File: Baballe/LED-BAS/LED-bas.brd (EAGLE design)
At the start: 30 x 32 mm, 12 parts, among them Q1 200mA/50V, Q2 200mA/50V, Q3 200mA/50V

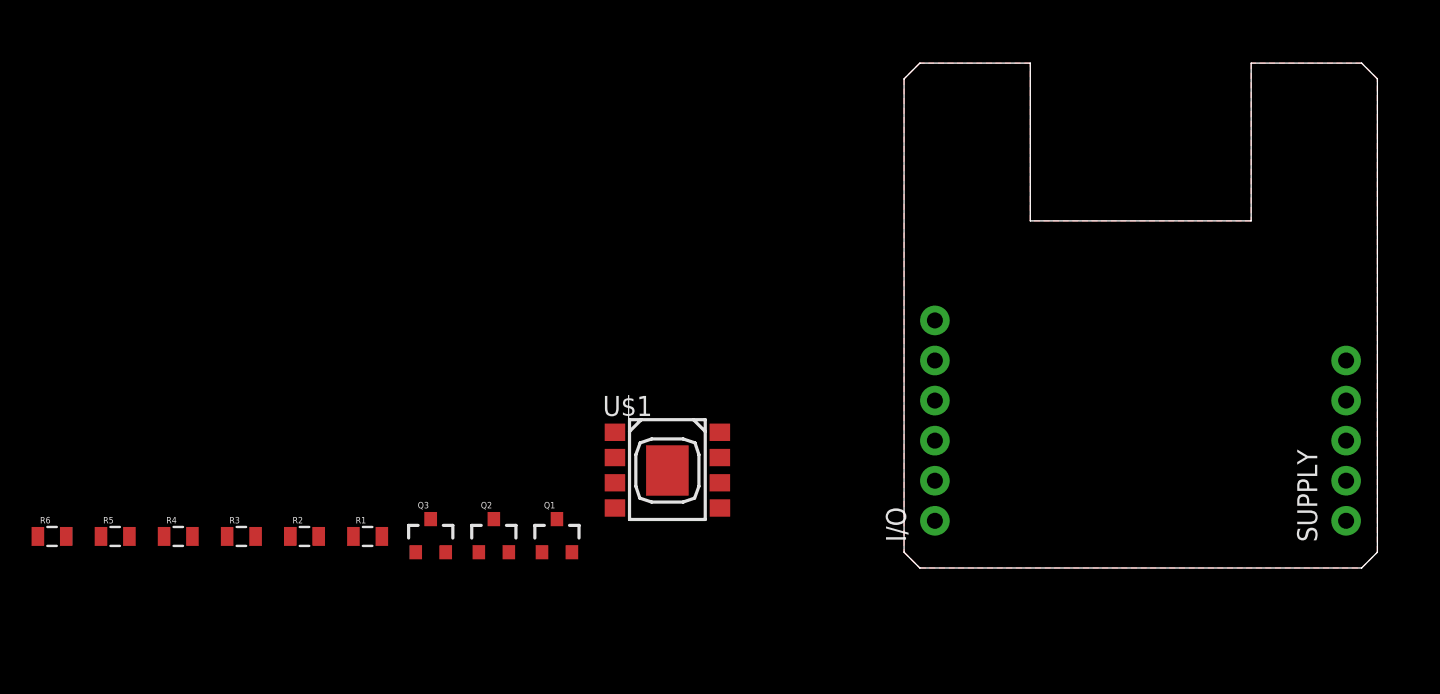
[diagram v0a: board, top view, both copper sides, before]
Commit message: Modification sur les modules led et alimentation
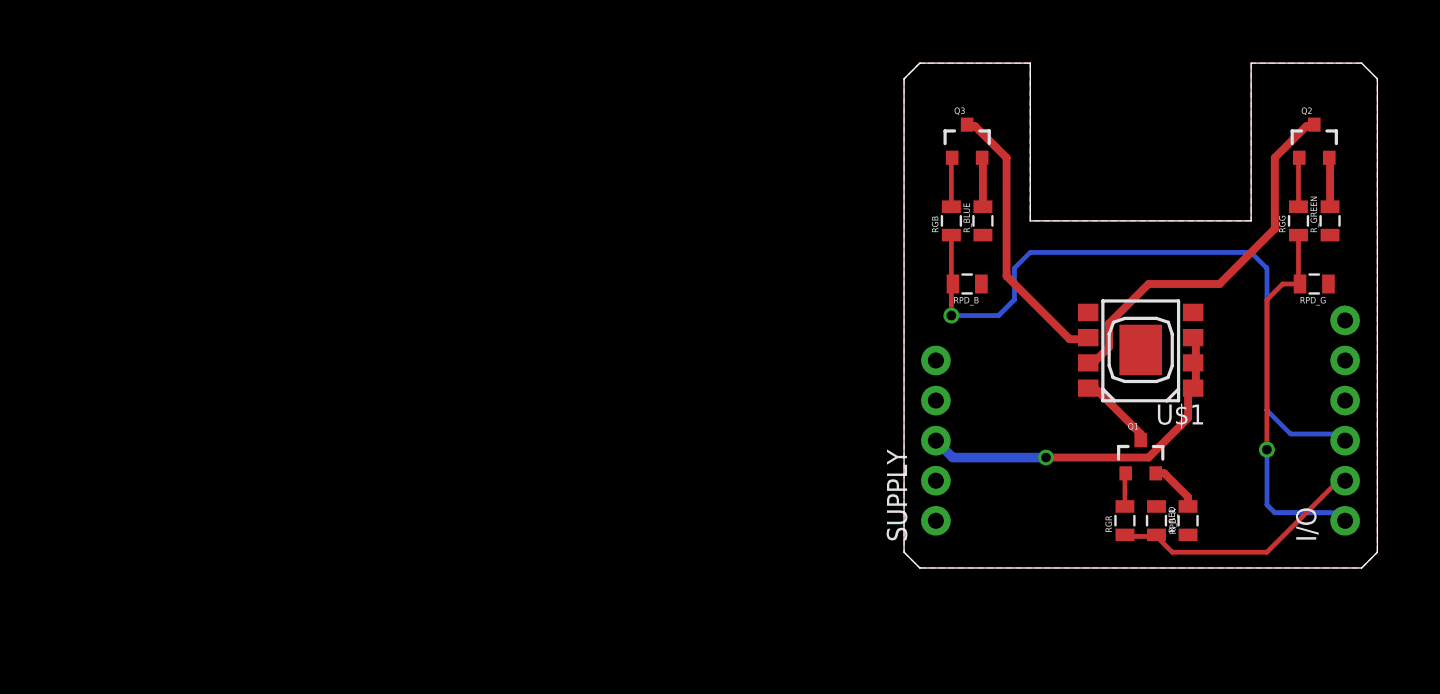
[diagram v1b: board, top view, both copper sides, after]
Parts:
- removed R1, R2, R3, R4, R5, R6: (no value), SparkFun-Resistors:0805
- added RGB, RGG, RGR: 1KOhm, SparkFun-Resistors:0805
- added RPD_B, RPD_G, RPD_R: 10KOhm, SparkFun-Resistors:0805
- added R_BLUE, R_GREEN, R_RED: 10Kohm, SparkFun-Resistors:0805
- I/O: value (none) -> I/O
- SUPPLY: value (none) -> SUPPLY
- moved Q2 57.7 mm to (70.0, 27.0)
- moved Q3 42.2 mm to (48.0, 27.0)
- moved Q1 37.3 mm to (59.0, 7.00)
- moved U$1 30.6 mm to (59.0, 13.0), turned to 180 degrees
- moved I/O 26.0 mm to (72.0, 2.99)
- moved SUPPLY 26.0 mm to (46.0, 2.99)
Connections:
- removed net I_BUTTON: I/O.4
- removed net I_VBAT: I/O.5
- removed net O_POWER_CTRL: I/O.6
- removed net VCC: SUPPLY.5
- removed net V_ALIM: SUPPLY.2
- removed net V_BAT: SUPPLY.4, U$1.2, U$1.4, U$1.6, U$1.8
- new net N$7: Q1.3, U$1.5
- new net N$8: Q2.3, U$1.6
- new net N$9: Q3.3, U$1.7
- net GND: now also RPD_B.1, RPD_G.1, RPD_R.1, R_BLUE.1, R_GREEN.1, R_RED.1; no longer R4.1, R5.1, R6.1
- net N$1: now also R_BLUE.2; no longer R6.2
- net N$2: now also R_GREEN.2; no longer R5.2
- net N$3: now also R_RED.2; no longer R4.2
- net N$4: now also RGG.2; no longer R3.2
- net N$5: now also RGR.2; no longer R2.2
- net N$6: now also RGB.2; no longer R1.2
- net O_BLUE: now also RGB.1, RPD_B.2; no longer R1.1
- net O_GREEN: now also RGG.1, RPD_G.2; no longer R3.1
- net O_RED: now also RGR.1, RPD_R.2; no longer R2.1
- net V_IN: now also U$1.1, U$1.2, U$1.3
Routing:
- net O_BLUE: track 0.00 -> 43.2 mm, vias 0 -> 1
- net O_GREEN: track 0.00 -> 24.4 mm, vias 0 -> 1
- net N$8: track 0.00 -> 24.2 mm
- net V_IN: track 0.00 -> 23.1 mm, vias 0 -> 1
- net N$9: track 0.00 -> 17.8 mm
- net O_RED: track 0.00 -> 16.5 mm
- net N$7: track 0.00 -> 4.98 mm
- net N$3: track 0.00 -> 3.27 mm
- net N$6: track 0.00 -> 3.15 mm
- net N$4: track 0.00 -> 3.15 mm
- net N$2: track 0.00 -> 3.15 mm
- net N$1: track 0.00 -> 3.15 mm
- net N$5: track 0.00 -> 2.15 mm
- added copper zone on layer 16, net GND

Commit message: V2 de la Baballe
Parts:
- moved Q2 26.1 mm to (56.0, 5.00)
- moved RGG 25.2 mm to (55.0, 1.00)
- moved RPD_G 20.2 mm to (59.0, 1.00), turned to 270 degrees
- moved R_GREEN 19.7 mm to (63.0, 4.00), turned to 180 degrees
- moved Q3 18.7 mm to (50.0, 8.37), turned to 270 degrees
- moved R_BLUE 15.1 mm to (47.0, 7.00)
- moved RPD_R 11.0 mm to (49.0, 4.00), turned to 90 degrees
- moved RGB 9.22 mm to (49.0, 13.0), turned to 270 degrees
- moved RGR 6.40 mm to (63.0, 7.00), turned to 180 degrees
- moved R_RED 6.08 mm to (63.0, 9.00), turned to 180 degrees
- moved I/O 4.03 mm to (68.0, 2.49)
- moved U$1 3.08 mm to (56.0, 13.7), turned to 270 degrees
- moved SUPPLY 2.31 mm to (43.9, 2.03)
- moved RPD_B 1.41 mm to (49.0, 17.0), turned to 270 degrees
- moved Q1 1.00 mm to (59.0, 8.00), turned to 90 degrees
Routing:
- net N$8: track 24.2 -> 4.28 mm
- net O_BLUE: track 43.2 -> 27.3 mm
- net N$9: track 17.8 -> 5.31 mm
- net O_RED: track 16.5 -> 25.6 mm, vias 0 -> 1
- net O_GREEN: track 24.4 -> 16.2 mm
- net V_IN: track 23.1 -> 27.0 mm
- net N$2: track 3.15 -> 5.15 mm
- net N$7: track 4.98 -> 3.04 mm
- net N$3: track 3.27 -> 2.15 mm
- net N$4: track 3.15 -> 2.15 mm
- net N$1: track 3.15 -> 2.58 mm
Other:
- board size 30 x 32 mm -> 36.1 x 36.1 mm

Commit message: Baballe en attente de vérification finale
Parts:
- moved I/O 0.50 mm to (68.0, 1.99)
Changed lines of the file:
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@@
 <setting verticaltext="up"/>
 </settings>
-<grid distance="0.1" unitdist="mm" unit="mm" style="lines" multiple="1" display="yes" altdistance="0.025" altunitdist="inch" altunit="inch"/>
+<grid distance="1" unitdist="mm" unit="mm" style="lines" multiple="1" display="yes" altdistance="0.025" altunitdist="inch" altunit="inch"/>
 <layers>
 <layer number="1" name="Top" color="4" fill="1" visible="yes" active="yes"/>
@@
 <layer number="45" name="Holes" color="7" fill="1" visible="yes" active="yes"/>
 <layer number="46" name="Milling" color="3" fill="1" visible="no" active="yes"/>
-<layer number="47" name="Measures" color="7" fill="1" visible="no" active="yes"/>
+<layer number="47" name="Measures" color="7" fill="1" visible="yes" active="yes"/>
 <layer number="48" name="Document" color="7" fill="1" visible="yes" active="yes"/>
 <layer number="49" name="Reference" color="7" fill="1" visible="yes" active="yes"/>
@@
 </autorouter>
 <elements>
-<element name="I/O" library="SparkFun-Connectors" package="1X06_NO_SILK" value="I/O" x="67.95533125" y="2.491" rot="R90">
-<attribute name="PROD_ID" value="CONN-08437" x="67.95533125" y="2.491" size="1.778" layer="27" rot="R90" display="off"/>
+<element name="I/O" library="SparkFun-Connectors" package="1X06_NO_SILK" value="I/O" x="68.00533125" y="1.991" rot="R90">
+<attribute name="PROD_ID" value="CONN-08437" x="68.00533125" y="1.991" size="1.778" layer="27" rot="R90" display="off"/>
 </element>
 <element name="SUPPLY" library="SparkFun-Connectors" package="1X05_NO_SILK" value="SUPPLY" x="43.9188625" y="2.026" rot="R90"/>
@@
 <wire x1="59" y1="2" x2="57" y2="0" width="0.3" layer="16"/>
 <wire x1="67.5" y1="2" x2="59" y2="2" width="0.3" layer="16"/>
-<wire x1="67.5" y1="2" x2="67.95533125" y2="2.491" width="0.3" layer="16"/>
+<wire x1="67.5" y1="2" x2="68.00533125" y2="1.991" width="0.3" layer="16"/>
 <via x="57" y="0" extent="1-16" drill="0.6096"/>
 </signal>
@@
 <wire x1="50.5" y1="14" x2="49" y2="14" width="0.3" layer="1"/>
 <wire x1="50.5" y1="8" x2="50.5" y2="14" width="0.3" layer="16"/>
-<wire x1="67.5" y1="8" x2="50.5" y2="8" width="0.3" layer="16"/>
+<wire x1="67" y1="8" x2="50.5" y2="8" width="0.3" layer="16"/>
 <wire x1="49" y1="14" x2="49" y2="13.9" width="0.3" layer="1"/>
-<wire x1="67.5" y1="8" x2="67.95533125" y2="7.571" width="0.3" layer="16"/>
+<wire x1="67" y1="8" x2="68.00533125" y2="7.071" width="0.3" layer="16"/>
 <via x="50.5" y="14" extent="1-16" drill="0.6096"/>
 </signal>
@@
 <wire x1="49.5" y1="5.5" x2="49" y2="6" width="0.3" layer="16"/>
 <wire x1="67.5" y1="5.5" x2="49.5" y2="5.5" width="0.3" layer="16"/>
-<wire x1="67.5" y1="5.5" x2="67.95533125" y2="5.031" width="0.3" layer="16"/>
-<wire x1="66" y1="7" x2="63.9" y2="7" width="0.3" layer="1"/>
-<wire x1="66" y1="6.5" x2="66" y2="7" width="0.3" layer="1"/>
-<wire x1="67.5" y1="5" x2="66" y2="6.5" width="0.3" layer="1"/>
-<wire x1="67.5" y1="5" x2="67.95533125" y2="5.031" width="0.3" layer="1"/>
+<wire x1="67.5" y1="5.5" x2="68.00533125" y2="4.531" width="0.3" layer="16"/>
+<wire x1="65" y1="7" x2="63.9" y2="7" width="0.3" layer="1"/>
+<wire x1="66" y1="6.5" x2="65" y2="7" width="0.3" layer="1"/>
+<wire x1="66" y1="6.5" x2="68.00533125" y2="4.531" width="0.3" layer="1"/>
 <via x="49" y="6" extent="1-16" drill="0.6096"/>
 </signal>
